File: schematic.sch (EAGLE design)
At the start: 7 parts

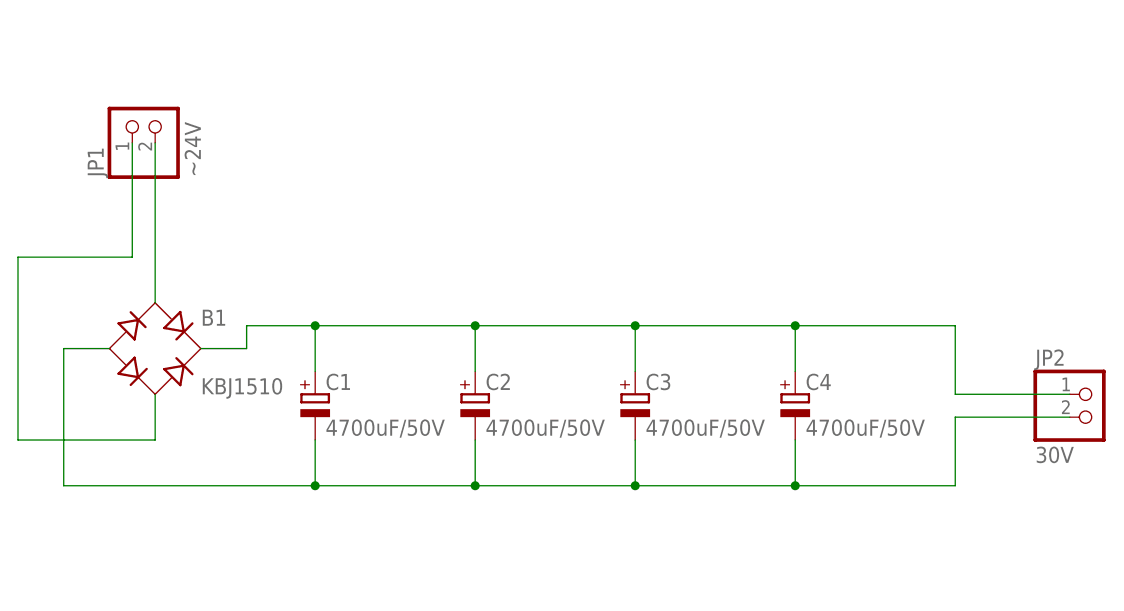
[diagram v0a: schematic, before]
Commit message: added power supply board
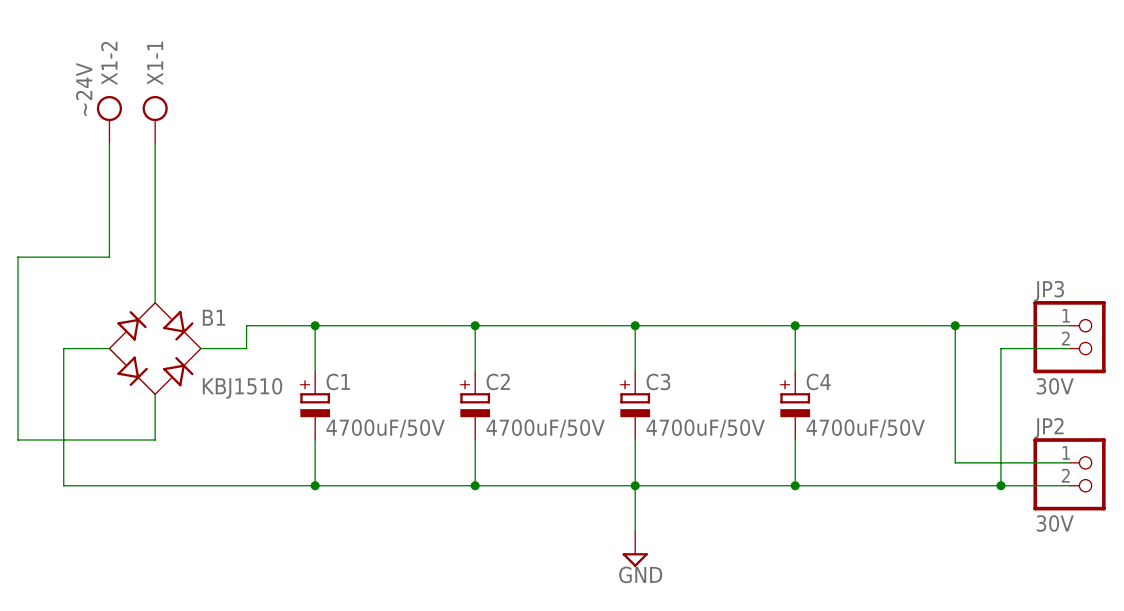
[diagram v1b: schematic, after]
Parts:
- removed JP1: ~24V, pinhead:PINHD-1X2
- added JP3: 30V, pinhead:PINHD-1X2
- added X1: ~24V, con-ptr500:AK500/2
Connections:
- removed net N$4: B1.-, C1.-, C2.-, C3.-, C4.-, JP2.2
- new net GND: B1.-, C1.-, C2.-, C3.-, C4.-, JP2.2, JP3.2
- net N$1: now also X1-2.KL; no longer JP1.1
- net N$2: now also X1-1.KL; no longer JP1.2
- net N$3: now also JP3.1
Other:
- moved on the sheet: JP2
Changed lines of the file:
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@@
 </classes>
 <parts>
-<part name="JP1" library="pinhead" deviceset="PINHD-1X2" device="" value="~24V"/>
 <part name="B1" library="rectifier" deviceset="RECTIFIER-" device="FB32" value="KBJ1510"/>
 <part name="C1" library="rcl" deviceset="CPOL-EU" device="E10-20" value="4700uF/50V"/>
@@
 <part name="C4" library="rcl" deviceset="CPOL-EU" device="E10-20" value="4700uF/50V"/>
 <part name="JP2" library="pinhead" deviceset="PINHD-1X2" device="" value="30V"/>
+<part name="JP3" library="pinhead" deviceset="PINHD-1X2" device="" value="30V"/>
+<part name="X1" library="con-ptr500" deviceset="AK500/2" device="" value="~24V"/>
+<part name="SUPPLY1" library="supply2" deviceset="GND" device=""/>
 </parts>
 <sheets>
@@
 </plain>
 <instances>
-<instance part="JP1" gate="G$1" x="-12.7" y="78.74" rot="R90"/>
 <instance part="B1" gate="G$1" x="-12.7" y="53.34"/>
 <instance part="C1" gate="G$1" x="5.08" y="48.26"/>
@@
 <instance part="C3" gate="G$1" x="40.64" y="48.26"/>
 <instance part="C4" gate="G$1" x="58.42" y="48.26"/>
-<instance part="JP2" gate="G$1" x="91.44" y="45.72"/>
+<instance part="JP2" gate="G$1" x="91.44" y="38.1"/>
+<instance part="JP3" gate="G$1" x="91.44" y="53.34"/>
+<instance part="X1" gate="-1" x="-12.7" y="81.28" rot="R270"/>
+<instance part="X1" gate="-2" x="-17.78" y="81.28" rot="R270"/>
+<instance part="SUPPLY1" gate="GND" x="40.64" y="30.48"/>
 </instances>
 <busses>
@@
 <net name="N$1" class="0">
 <segment>
-<pinref part="JP1" gate="G$1" pin="1"/>
-<wire x1="-15.24" y1="76.2" x2="-15.24" y2="63.5" width="0.1524" layer="91"/>
-<wire x1="-15.24" y1="63.5" x2="-27.94" y2="63.5" width="0.1524" layer="91"/>
+<wire x1="-17.78" y1="76.2" x2="-17.78" y2="63.5" width="0.1524" layer="91"/>
+<wire x1="-17.78" y1="63.5" x2="-27.94" y2="63.5" width="0.1524" layer="91"/>
 <wire x1="-27.94" y1="63.5" x2="-27.94" y2="43.18" width="0.1524" layer="91"/>
 <pinref part="B1" gate="G$1" pin="AC2"/>
 <wire x1="-27.94" y1="43.18" x2="-12.7" y2="43.18" width="0.1524" layer="91"/>
 <wire x1="-12.7" y1="43.18" x2="-12.7" y2="48.26" width="0.1524" layer="91"/>
+<pinref part="X1" gate="-2" pin="KL"/>
 </segment>
 </net>
@@
 <segment>
 <pinref part="B1" gate="G$1" pin="AC1"/>
-<pinref part="JP1" gate="G$1" pin="2"/>
 <wire x1="-12.7" y1="58.42" x2="-12.7" y2="76.2" width="0.1524" layer="91"/>
+<pinref part="X1" gate="-1" pin="KL"/>
 </segment>
 </net>
@@
 <junction x="5.08" y="55.88"/>
 <wire x1="58.42" y1="55.88" x2="76.2" y2="55.88" width="0.1524" layer="91"/>
-<wire x1="76.2" y1="55.88" x2="76.2" y2="48.26" width="0.1524" layer="91"/>
+<wire x1="76.2" y1="55.88" x2="76.2" y2="40.64" width="0.1524" layer="91"/>
 <junction x="58.42" y="55.88"/>
 <pinref part="JP2" gate="G$1" pin="1"/>
-<wire x1="76.2" y1="48.26" x2="88.9" y2="48.26" width="0.1524" layer="91"/>
+<wire x1="76.2" y1="40.64" x2="88.9" y2="40.64" width="0.1524" layer="91"/>
+<pinref part="JP3" gate="G$1" pin="1"/>
+<wire x1="88.9" y1="55.88" x2="76.2" y2="55.88" width="0.1524" layer="91"/>
+<junction x="76.2" y="55.88"/>
 </segment>
 </net>
-<net name="N$4" class="0">
+<net name="GND" class="0">
 <segment>
 <pinref part="B1" gate="G$1" pin="-"/>
@@
 <junction x="40.64" y="38.1"/>
 <pinref part="JP2" gate="G$1" pin="2"/>
-<wire x1="88.9" y1="45.72" x2="76.2" y2="45.72" width="0.1524" layer="91"/>
-<wire x1="76.2" y1="45.72" x2="76.2" y2="38.1" width="0.1524" layer="91"/>
-<wire x1="76.2" y1="38.1" x2="58.42" y2="38.1" width="0.1524" layer="91"/>
+<wire x1="88.9" y1="38.1" x2="81.28" y2="38.1" width="0.1524" layer="91"/>
 <junction x="58.42" y="38.1"/>
+<pinref part="JP3" gate="G$1" pin="2"/>
+<wire x1="81.28" y1="38.1" x2="58.42" y2="38.1" width="0.1524" layer="91"/>
+<wire x1="88.9" y1="53.34" x2="81.28" y2="53.34" width="0.1524" layer="91"/>
+<wire x1="81.28" y1="53.34" x2="81.28" y2="38.1" width="0.1524" layer="91"/>
+<junction x="81.28" y="38.1"/>
+<pinref part="SUPPLY1" gate="GND" pin="GND"/>
+<wire x1="40.64" y1="33.02" x2="40.64" y2="38.1" width="0.1524" layer="91"/>
 </segment>
 </net>
